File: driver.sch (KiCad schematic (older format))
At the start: 11 parts, among them U5 L6201PS

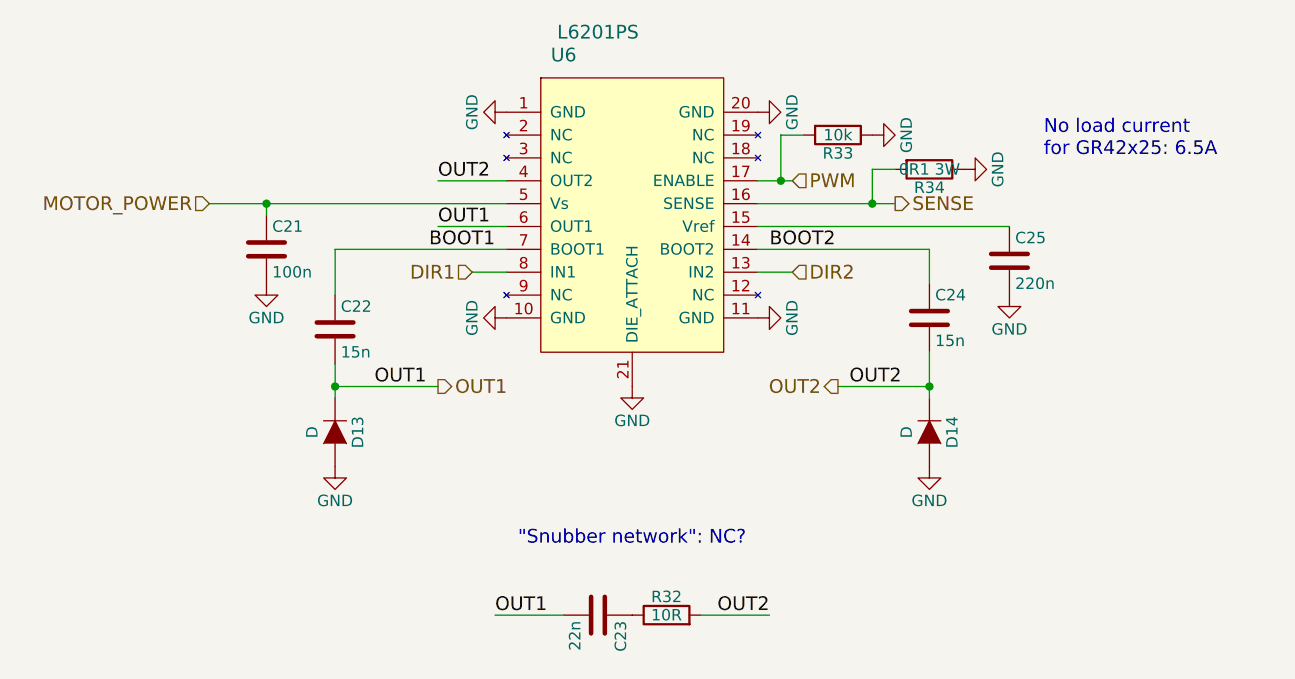
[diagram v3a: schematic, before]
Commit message: Partial footprint association
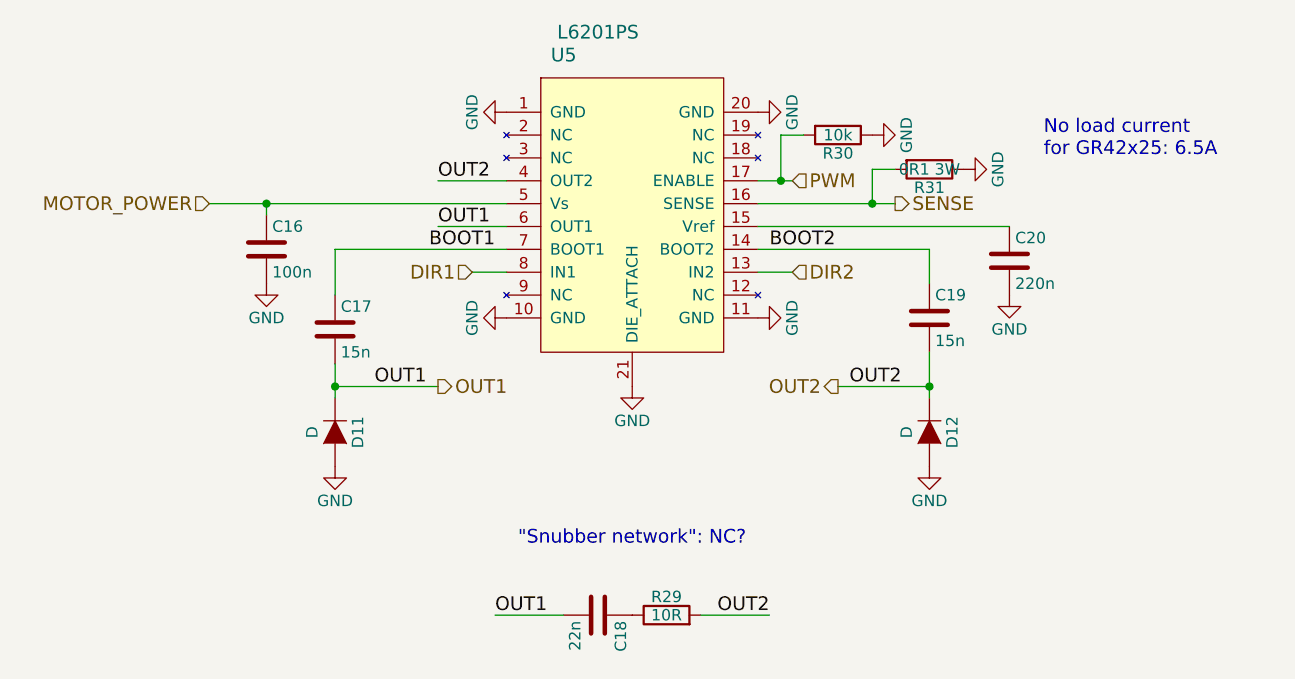
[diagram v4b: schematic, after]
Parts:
- C16, C17, C18, C19, C20, R29, R30: footprint (none) -> hexabot:R_0805_HandSoldering
- R31: footprint (none) -> hexabot:R_1206_HandSoldering
- U5: footprint (none) -> hexabot:powerso-20
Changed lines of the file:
@@
 AR Path="/5578F5CB/557880D8" Ref="U6"  Part="1"
 AR Path="/557880D8" Ref="U5"  Part="1"
-F 0 "U6" H 5400 3850 60  0000 C CNN
+F 0 "U5" H 5400 3850 60  0000 C CNN
 F 1 "L6201PS" H 5550 3950 60  0000 C CNN
-F 2 "" H 5300 3750 60  0000 C CNN
+F 2 "hexabot:powerso-20" H 5300 3750 60  0001 C CNN
 F 3 "" H 5300 3750 60  0000 C CNN
 	1    5700 3200
@@
 $EndComp
 $Comp
-L GND #PWR79
+L GND #PWR076
 U 1 1 557880DF
 P 6250 3700
-AR Path="/5578B32E/557880DF" Ref="#PWR79"  Part="1"
-AR Path="/5578F5CB/557880DF" Ref="#PWR90"  Part="1"
-F 0 "#PWR90" H 6250 3450 50  0001 C CNN
+AR Path="/5578B32E/557880DF" Ref="#PWR076"  Part="1"
+AR Path="/5578F5CB/557880DF" Ref="#PWR087"  Part="1"
+F 0 "#PWR076" H 6250 3450 50  0001 C CNN
 F 1 "GND" H 6250 3550 50  0000 C CNN
 F 2 "" H 6250 3700 60  0000 C CNN
@@
 $EndComp
 $Comp
-L GND #PWR78
+L GND #PWR077
 U 1 1 557880E5
 P 6250 2800
-AR Path="/5578B32E/557880E5" Ref="#PWR78"  Part="1"
-AR Path="/5578F5CB/557880E5" Ref="#PWR89"  Part="1"
-F 0 "#PWR89" H 6250 2550 50  0001 C CNN
+AR Path="/5578B32E/557880E5" Ref="#PWR077"  Part="1"
+AR Path="/5578F5CB/557880E5" Ref="#PWR088"  Part="1"
+F 0 "#PWR077" H 6250 2550 50  0001 C CNN
 F 1 "GND" H 6250 2650 50  0000 C CNN
 F 2 "" H 6250 2800 60  0000 C CNN
@@
 $EndComp
 $Comp
-L GND #PWR75
+L GND #PWR078
 U 1 1 557880EB
 P 5150 2800
-AR Path="/5578B32E/557880EB" Ref="#PWR75"  Part="1"
-AR Path="/5578F5CB/557880EB" Ref="#PWR86"  Part="1"
-F 0 "#PWR86" H 5150 2550 50  0001 C CNN
+AR Path="/5578B32E/557880EB" Ref="#PWR078"  Part="1"
+AR Path="/5578F5CB/557880EB" Ref="#PWR089"  Part="1"
+F 0 "#PWR078" H 5150 2550 50  0001 C CNN
 F 1 "GND" H 5150 2650 50  0000 C CNN
 F 2 "" H 5150 2800 60  0000 C CNN
@@
 $EndComp
 $Comp
-L GND #PWR76
+L GND #PWR079
 U 1 1 557880F1
 P 5150 3700
-AR Path="/5578B32E/557880F1" Ref="#PWR76"  Part="1"
-AR Path="/5578F5CB/557880F1" Ref="#PWR87"  Part="1"
-F 0 "#PWR87" H 5150 3450 50  0001 C CNN
+AR Path="/5578B32E/557880F1" Ref="#PWR079"  Part="1"
+AR Path="/5578F5CB/557880F1" Ref="#PWR090"  Part="1"
+F 0 "#PWR079" H 5150 3450 50  0001 C CNN
 F 1 "GND" H 5150 3550 50  0000 C CNN
 F 2 "" H 5150 3700 60  0000 C CNN
@@
 AR Path="/5578B32E/55788105" Ref="C16"  Part="1"
 AR Path="/5578F5CB/55788105" Ref="C21"  Part="1"
-F 0 "C21" H 4125 3500 50  0000 L CNN
+F 0 "C16" H 4125 3500 50  0000 L CNN
 F 1 "100n" H 4125 3300 50  0000 L CNN
-F 2 "" H 4138 3250 30  0000 C CNN
+F 2 "hexabot:R_0805_HandSoldering" H 4138 3250 30  0001 C CNN
 F 3 "" H 4100 3400 60  0000 C CNN
 	1    4100 3400
@@
 $EndComp
 $Comp
-L GND #PWR73
+L GND #PWR080
 U 1 1 5578810C
 P 4100 3550
-AR Path="/5578B32E/5578810C" Ref="#PWR73"  Part="1"
-AR Path="/5578F5CB/5578810C" Ref="#PWR84"  Part="1"
-F 0 "#PWR84" H 4100 3300 50  0001 C CNN
+AR Path="/5578B32E/5578810C" Ref="#PWR080"  Part="1"
+AR Path="/5578F5CB/5578810C" Ref="#PWR091"  Part="1"
+F 0 "#PWR080" H 4100 3300 50  0001 C CNN
 F 1 "GND" H 4100 3400 50  0000 C CNN
 F 2 "" H 4100 3550 60  0000 C CNN
@@
 AR Path="/5578B32E/5578811A" Ref="C17"  Part="1"
 AR Path="/5578F5CB/5578811A" Ref="C22"  Part="1"
-F 0 "C22" H 4425 3850 50  0000 L CNN
+F 0 "C17" H 4425 3850 50  0000 L CNN
 F 1 "15n" H 4425 3650 50  0000 L CNN
-F 2 "" H 4438 3600 30  0000 C CNN
+F 2 "hexabot:R_0805_HandSoldering" H 4438 3600 30  0001 C CNN
 F 3 "" H 4400 3750 60  0000 C CNN
 	1    4400 3750
@@
 AR Path="/5578B32E/55788121" Ref="C19"  Part="1"
 AR Path="/5578F5CB/55788121" Ref="C24"  Part="1"
-F 0 "C24" H 7025 3800 50  0000 L CNN
+F 0 "C19" H 7025 3800 50  0000 L CNN
 F 1 "15n" H 7025 3600 50  0000 L CNN
-F 2 "" H 7038 3550 30  0000 C CNN
+F 2 "hexabot:R_0805_HandSoldering" H 7038 3550 30  0001 C CNN
 F 3 "" H 7000 3700 60  0000 C CNN
 	1    7000 3700
@@
 AR Path="/5578B32E/55788757" Ref="R31"  Part="1"
 AR Path="/5578F5CB/55788757" Ref="R34"  Part="1"
-F 0 "R34" V 7080 3050 50  0000 C CNN
+F 0 "R31" V 7080 3050 50  0000 C CNN
 F 1 "0R1 3W" V 7000 3050 50  0000 C CNN
-F 2 "" V 6930 3050 30  0000 C CNN
+F 2 "hexabot:R_1206_HandSoldering" V 6930 3050 30  0001 C CNN
 F 3 "" H 7000 3050 30  0000 C CNN
 	1    7000 3050
@@
 SENSE
 $Comp
-L GND #PWR82
+L GND #PWR081
 U 1 1 557887AF
 P 7150 3050
-AR Path="/5578B32E/557887AF" Ref="#PWR82"  Part="1"
-AR Path="/5578F5CB/557887AF" Ref="#PWR93"  Part="1"
-F 0 "#PWR93" H 7150 2800 50  0001 C CNN
+AR Path="/5578B32E/557887AF" Ref="#PWR081"  Part="1"
+AR Path="/5578F5CB/557887AF" Ref="#PWR092"  Part="1"
+F 0 "#PWR081" H 7150 2800 50  0001 C CNN
 F 1 "GND" H 7150 2900 50  0000 C CNN
 F 2 "" H 7150 3050 60  0000 C CNN
@@
 AR Path="/5578B32E/55788975" Ref="C18"  Part="1"
 AR Path="/5578F5CB/55788975" Ref="C23"  Part="1"
-F 0 "C23" H 5575 5100 50  0000 L CNN
+F 0 "C18" H 5575 5100 50  0000 L CNN
 F 1 "22n" H 5575 4900 50  0000 L CNN
-F 2 "" H 5588 4850 30  0000 C CNN
+F 2 "hexabot:R_0805_HandSoldering" H 5588 4850 30  0001 C CNN
 F 3 "" H 5550 5000 60  0000 C CNN
 	1    5550 5000
@@
 AR Path="/5578B32E/557889B4" Ref="R29"  Part="1"
 AR Path="/5578F5CB/557889B4" Ref="R32"  Part="1"
-F 0 "R32" V 5930 5000 50  0000 C CNN
+F 0 "R29" V 5930 5000 50  0000 C CNN
 F 1 "10R" V 5850 5000 50  0000 C CNN
-F 2 "" V 5780 5000 30  0000 C CNN
+F 2 "hexabot:R_0805_HandSoldering" V 5780 5000 30  0001 C CNN
 F 3 "" H 5850 5000 30  0000 C CNN
 	1    5850 5000
@@
 AR Path="/5578B32E/55788DDE" Ref="D11"  Part="1"
 AR Path="/5578F5CB/55788DDE" Ref="D13"  Part="1"
-F 0 "D13" H 4400 4300 50  0000 C CNN
+F 0 "D11" H 4400 4300 50  0000 C CNN
 F 1 "D" H 4400 4100 50  0000 C CNN
-F 2 "" H 4400 4200 60  0000 C CNN
+F 2 "" H 4400 4200 60  0001 C CNN
 F 3 "" H 4400 4200 60  0000 C CNN
 	1    4400 4200
@@
 AR Path="/5578B32E/55788E84" Ref="D12"  Part="1"
 AR Path="/5578F5CB/55788E84" Ref="D14"  Part="1"
-F 0 "D14" H 7000 4300 50  0000 C CNN
+F 0 "D12" H 7000 4300 50  0000 C CNN
 F 1 "D" H 7000 4100 50  0000 C CNN
-F 2 "" H 7000 4200 60  0000 C CNN
+F 2 "" H 7000 4200 60  0001 C CNN
 F 3 "" H 7000 4200 60  0000 C CNN
 	1    7000 4200
@@
 Connection ~ 4400 4000
 $Comp
-L GND #PWR74
+L GND #PWR082
 U 1 1 55788F78
 P 4400 4350
-AR Path="/5578B32E/55788F78" Ref="#PWR74"  Part="1"
-AR Path="/5578F5CB/55788F78" Ref="#PWR85"  Part="1"
-F 0 "#PWR85" H 4400 4100 50  0001 C CNN
+AR Path="/5578B32E/55788F78" Ref="#PWR082"  Part="1"
+AR Path="/5578F5CB/55788F78" Ref="#PWR093"  Part="1"
+F 0 "#PWR082" H 4400 4100 50  0001 C CNN
 F 1 "GND" H 4400 4200 50  0000 C CNN
 F 2 "" H 4400 4350 60  0000 C CNN
@@
 $EndComp
 $Comp
-L GND #PWR81
+L GND #PWR083
 U 1 1 55788FAE
 P 7000 4350
-AR Path="/5578B32E/55788FAE" Ref="#PWR81"  Part="1"
-AR Path="/5578F5CB/55788FAE" Ref="#PWR92"  Part="1"
-F 0 "#PWR92" H 7000 4100 50  0001 C CNN
+AR Path="/5578B32E/55788FAE" Ref="#PWR083"  Part="1"
+AR Path="/5578F5CB/55788FAE" Ref="#PWR094"  Part="1"
+F 0 "#PWR083" H 7000 4100 50  0001 C CNN
 F 1 "GND" H 7000 4200 50  0000 C CNN
 F 2 "" H 7000 4350 60  0000 C CNN
@@
 AR Path="/5578B32E/55789138" Ref="C20"  Part="1"
 AR Path="/5578F5CB/55789138" Ref="C25"  Part="1"
-F 0 "C25" H 7375 3550 50  0000 L CNN
+F 0 "C20" H 7375 3550 50  0000 L CNN
 F 1 "220n" H 7375 3350 50  0000 L CNN
-F 2 "" H 7388 3300 30  0000 C CNN
+F 2 "hexabot:R_0805_HandSoldering" H 7388 3300 30  0001 C CNN
 F 3 "" H 7350 3450 60  0000 C CNN
 	1    7350 3450
@@
 $EndComp
 $Comp
-L GND #PWR83
+L GND #PWR084
 U 1 1 55789189
 P 7350 3600
-AR Path="/5578B32E/55789189" Ref="#PWR83"  Part="1"
-AR Path="/5578F5CB/55789189" Ref="#PWR94"  Part="1"
-F 0 "#PWR94" H 7350 3350 50  0001 C CNN
+AR Path="/5578B32E/55789189" Ref="#PWR084"  Part="1"
+AR Path="/5578F5CB/55789189" Ref="#PWR095"  Part="1"
+F 0 "#PWR084" H 7350 3350 50  0001 C CNN
 F 1 "GND" H 7350 3450 50  0000 C CNN
 F 2 "" H 7350 3600 60  0000 C CNN
@@
 AR Path="/5578B32E/55798ABA" Ref="R30"  Part="1"
 AR Path="/5578F5CB/55798ABA" Ref="R33"  Part="1"
-F 0 "R33" V 6680 2900 50  0000 C CNN
+F 0 "R30" V 6680 2900 50  0000 C CNN
 F 1 "10k" V 6600 2900 50  0000 C CNN
-F 2 "" V 6530 2900 30  0000 C CNN
+F 2 "hexabot:R_0805_HandSoldering" V 6530 2900 30  0001 C CNN
 F 3 "" H 6600 2900 30  0000 C CNN
 	1    6600 2900
@@
 	6350 2900 6450 2900
 $Comp
-L GND #PWR80
+L GND #PWR085
 U 1 1 55798BC1
 P 6750 2900
-AR Path="/5578B32E/55798BC1" Ref="#PWR80"  Part="1"
-AR Path="/5578F5CB/55798BC1" Ref="#PWR91"  Part="1"
-F 0 "#PWR91" H 6750 2650 50  0001 C CNN
+AR Path="/5578B32E/55798BC1" Ref="#PWR085"  Part="1"
+AR Path="/5578F5CB/55798BC1" Ref="#PWR096"  Part="1"
+F 0 "#PWR085" H 6750 2650 50  0001 C CNN
 F 1 "GND" H 6750 2750 50  0000 C CNN
 F 2 "" H 6750 2900 60  0000 C CNN
@@
 No load current\nfor GR42x25: 6.5A
 $Comp
-L GND #PWR77
+L GND #PWR086
 U 1 1 557A2B97
 P 5700 4000
-AR Path="/5578B32E/557A2B97" Ref="#PWR77"  Part="1"
-AR Path="/5578F5CB/557A2B97" Ref="#PWR88"  Part="1"
-F 0 "#PWR88" H 5700 3750 50  0001 C CNN
+AR Path="/5578B32E/557A2B97" Ref="#PWR086"  Part="1"
+AR Path="/5578F5CB/557A2B97" Ref="#PWR097"  Part="1"
+F 0 "#PWR086" H 5700 3750 50  0001 C CNN
 F 1 "GND" H 5700 3850 50  0000 C CNN
 F 2 "" H 5700 4000 60  0000 C CNN

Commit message: Remove KK for motors
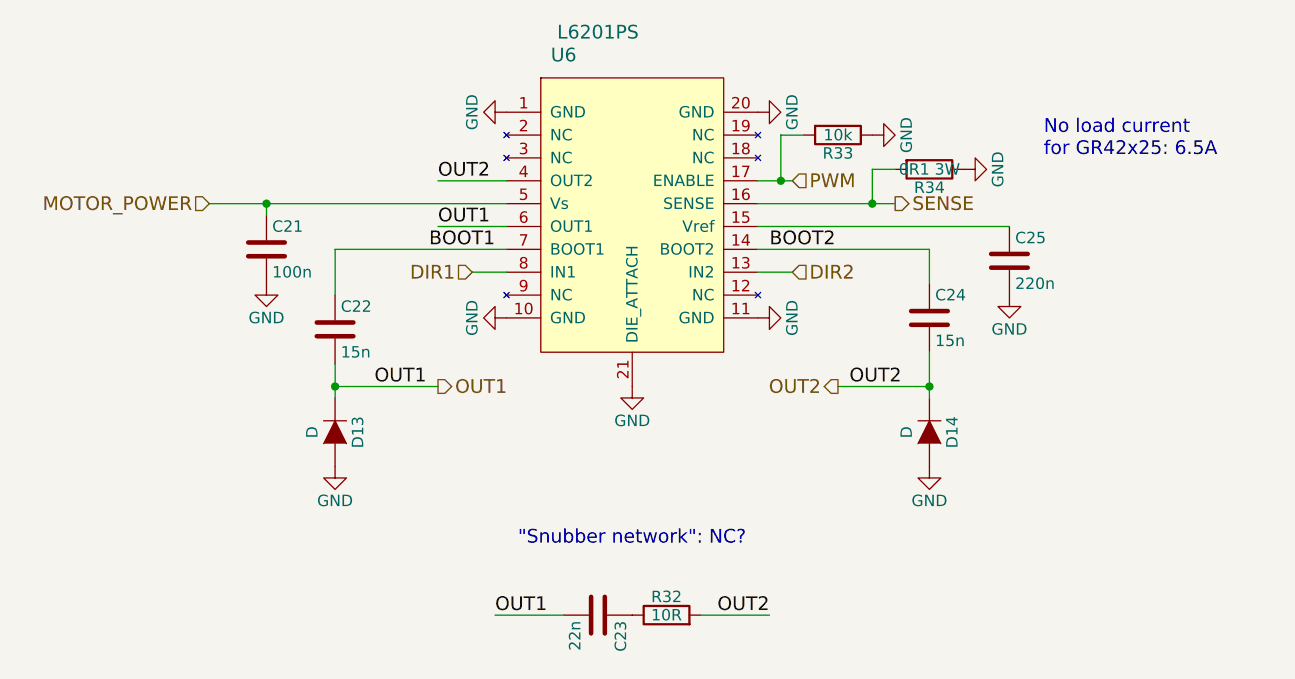
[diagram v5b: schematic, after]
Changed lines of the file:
@@
 AR Path="/5578F5CB/557880D8" Ref="U6"  Part="1"
 AR Path="/557880D8" Ref="U5"  Part="1"
-F 0 "U5" H 5400 3850 60  0000 C CNN
+F 0 "U6" H 5400 3850 60  0000 C CNN
 F 1 "L6201PS" H 5550 3950 60  0000 C CNN
 F 2 "hexabot:powerso-20" H 5300 3750 60  0001 C CNN
@@
 AR Path="/5578B32E/557880DF" Ref="#PWR076"  Part="1"
 AR Path="/5578F5CB/557880DF" Ref="#PWR087"  Part="1"
-F 0 "#PWR076" H 6250 3450 50  0001 C CNN
+F 0 "#PWR087" H 6250 3450 50  0001 C CNN
 F 1 "GND" H 6250 3550 50  0000 C CNN
 F 2 "" H 6250 3700 60  0000 C CNN
@@
 AR Path="/5578B32E/557880E5" Ref="#PWR077"  Part="1"
 AR Path="/5578F5CB/557880E5" Ref="#PWR088"  Part="1"
-F 0 "#PWR077" H 6250 2550 50  0001 C CNN
+F 0 "#PWR088" H 6250 2550 50  0001 C CNN
 F 1 "GND" H 6250 2650 50  0000 C CNN
 F 2 "" H 6250 2800 60  0000 C CNN
@@
 AR Path="/5578B32E/557880EB" Ref="#PWR078"  Part="1"
 AR Path="/5578F5CB/557880EB" Ref="#PWR089"  Part="1"
-F 0 "#PWR078" H 5150 2550 50  0001 C CNN
+F 0 "#PWR089" H 5150 2550 50  0001 C CNN
 F 1 "GND" H 5150 2650 50  0000 C CNN
 F 2 "" H 5150 2800 60  0000 C CNN
@@
 AR Path="/5578B32E/557880F1" Ref="#PWR079"  Part="1"
 AR Path="/5578F5CB/557880F1" Ref="#PWR090"  Part="1"
-F 0 "#PWR079" H 5150 3450 50  0001 C CNN
+F 0 "#PWR090" H 5150 3450 50  0001 C CNN
 F 1 "GND" H 5150 3550 50  0000 C CNN
 F 2 "" H 5150 3700 60  0000 C CNN
@@
 AR Path="/5578B32E/55788105" Ref="C16"  Part="1"
 AR Path="/5578F5CB/55788105" Ref="C21"  Part="1"
-F 0 "C16" H 4125 3500 50  0000 L CNN
+F 0 "C21" H 4125 3500 50  0000 L CNN
 F 1 "100n" H 4125 3300 50  0000 L CNN
 F 2 "hexabot:R_0805_HandSoldering" H 4138 3250 30  0001 C CNN
@@
 AR Path="/5578B32E/5578810C" Ref="#PWR080"  Part="1"
 AR Path="/5578F5CB/5578810C" Ref="#PWR091"  Part="1"
-F 0 "#PWR080" H 4100 3300 50  0001 C CNN
+F 0 "#PWR091" H 4100 3300 50  0001 C CNN
 F 1 "GND" H 4100 3400 50  0000 C CNN
 F 2 "" H 4100 3550 60  0000 C CNN
@@
 AR Path="/5578B32E/5578811A" Ref="C17"  Part="1"
 AR Path="/5578F5CB/5578811A" Ref="C22"  Part="1"
-F 0 "C17" H 4425 3850 50  0000 L CNN
+F 0 "C22" H 4425 3850 50  0000 L CNN
 F 1 "15n" H 4425 3650 50  0000 L CNN
 F 2 "hexabot:R_0805_HandSoldering" H 4438 3600 30  0001 C CNN
@@
 AR Path="/5578B32E/55788121" Ref="C19"  Part="1"
 AR Path="/5578F5CB/55788121" Ref="C24"  Part="1"
-F 0 "C19" H 7025 3800 50  0000 L CNN
+F 0 "C24" H 7025 3800 50  0000 L CNN
 F 1 "15n" H 7025 3600 50  0000 L CNN
 F 2 "hexabot:R_0805_HandSoldering" H 7038 3550 30  0001 C CNN
@@
 AR Path="/5578B32E/55788757" Ref="R31"  Part="1"
 AR Path="/5578F5CB/55788757" Ref="R34"  Part="1"
-F 0 "R31" V 7080 3050 50  0000 C CNN
+F 0 "R34" V 7080 3050 50  0000 C CNN
 F 1 "0R1 3W" V 7000 3050 50  0000 C CNN
 F 2 "hexabot:R_1206_HandSoldering" V 6930 3050 30  0001 C CNN
@@
 AR Path="/5578B32E/557887AF" Ref="#PWR081"  Part="1"
 AR Path="/5578F5CB/557887AF" Ref="#PWR092"  Part="1"
-F 0 "#PWR081" H 7150 2800 50  0001 C CNN
+F 0 "#PWR092" H 7150 2800 50  0001 C CNN
 F 1 "GND" H 7150 2900 50  0000 C CNN
 F 2 "" H 7150 3050 60  0000 C CNN
@@
 AR Path="/5578B32E/55788975" Ref="C18"  Part="1"
 AR Path="/5578F5CB/55788975" Ref="C23"  Part="1"
-F 0 "C18" H 5575 5100 50  0000 L CNN
+F 0 "C23" H 5575 5100 50  0000 L CNN
 F 1 "22n" H 5575 4900 50  0000 L CNN
 F 2 "hexabot:R_0805_HandSoldering" H 5588 4850 30  0001 C CNN
@@
 AR Path="/5578B32E/557889B4" Ref="R29"  Part="1"
 AR Path="/5578F5CB/557889B4" Ref="R32"  Part="1"
-F 0 "R29" V 5930 5000 50  0000 C CNN
+F 0 "R32" V 5930 5000 50  0000 C CNN
 F 1 "10R" V 5850 5000 50  0000 C CNN
 F 2 "hexabot:R_0805_HandSoldering" V 5780 5000 30  0001 C CNN
@@
 AR Path="/5578B32E/55788DDE" Ref="D11"  Part="1"
 AR Path="/5578F5CB/55788DDE" Ref="D13"  Part="1"
-F 0 "D11" H 4400 4300 50  0000 C CNN
+F 0 "D13" H 4400 4300 50  0000 C CNN
 F 1 "D" H 4400 4100 50  0000 C CNN
 F 2 "" H 4400 4200 60  0001 C CNN
@@
 AR Path="/5578B32E/55788E84" Ref="D12"  Part="1"
 AR Path="/5578F5CB/55788E84" Ref="D14"  Part="1"
-F 0 "D12" H 7000 4300 50  0000 C CNN
+F 0 "D14" H 7000 4300 50  0000 C CNN
 F 1 "D" H 7000 4100 50  0000 C CNN
 F 2 "" H 7000 4200 60  0001 C CNN
@@
 AR Path="/5578B32E/55788F78" Ref="#PWR082"  Part="1"
 AR Path="/5578F5CB/55788F78" Ref="#PWR093"  Part="1"
-F 0 "#PWR082" H 4400 4100 50  0001 C CNN
+F 0 "#PWR093" H 4400 4100 50  0001 C CNN
 F 1 "GND" H 4400 4200 50  0000 C CNN
 F 2 "" H 4400 4350 60  0000 C CNN
@@
 AR Path="/5578B32E/55788FAE" Ref="#PWR083"  Part="1"
 AR Path="/5578F5CB/55788FAE" Ref="#PWR094"  Part="1"
-F 0 "#PWR083" H 7000 4100 50  0001 C CNN
+F 0 "#PWR094" H 7000 4100 50  0001 C CNN
 F 1 "GND" H 7000 4200 50  0000 C CNN
 F 2 "" H 7000 4350 60  0000 C CNN
@@
 AR Path="/5578B32E/55789138" Ref="C20"  Part="1"
 AR Path="/5578F5CB/55789138" Ref="C25"  Part="1"
-F 0 "C20" H 7375 3550 50  0000 L CNN
+F 0 "C25" H 7375 3550 50  0000 L CNN
 F 1 "220n" H 7375 3350 50  0000 L CNN
 F 2 "hexabot:R_0805_HandSoldering" H 7388 3300 30  0001 C CNN
@@
 AR Path="/5578B32E/55789189" Ref="#PWR084"  Part="1"
 AR Path="/5578F5CB/55789189" Ref="#PWR095"  Part="1"
-F 0 "#PWR084" H 7350 3350 50  0001 C CNN
+F 0 "#PWR095" H 7350 3350 50  0001 C CNN
 F 1 "GND" H 7350 3450 50  0000 C CNN
 F 2 "" H 7350 3600 60  0000 C CNN
@@
 AR Path="/5578B32E/55798ABA" Ref="R30"  Part="1"
 AR Path="/5578F5CB/55798ABA" Ref="R33"  Part="1"
-F 0 "R30" V 6680 2900 50  0000 C CNN
+F 0 "R33" V 6680 2900 50  0000 C CNN
 F 1 "10k" V 6600 2900 50  0000 C CNN
 F 2 "hexabot:R_0805_HandSoldering" V 6530 2900 30  0001 C CNN
@@
 AR Path="/5578B32E/55798BC1" Ref="#PWR085"  Part="1"
 AR Path="/5578F5CB/55798BC1" Ref="#PWR096"  Part="1"
-F 0 "#PWR085" H 6750 2650 50  0001 C CNN
+F 0 "#PWR096" H 6750 2650 50  0001 C CNN
 F 1 "GND" H 6750 2750 50  0000 C CNN
 F 2 "" H 6750 2900 60  0000 C CNN
@@
 AR Path="/5578B32E/557A2B97" Ref="#PWR086"  Part="1"
 AR Path="/5578F5CB/557A2B97" Ref="#PWR097"  Part="1"
-F 0 "#PWR086" H 5700 3750 50  0001 C CNN
+F 0 "#PWR097" H 5700 3750 50  0001 C CNN
 F 1 "GND" H 5700 3850 50  0000 C CNN
 F 2 "" H 5700 4000 60  0000 C CNN
